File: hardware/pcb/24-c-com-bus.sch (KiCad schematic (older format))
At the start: 5 parts

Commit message: Created variants
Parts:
- C401: renamed from C?; Config (none) -> -MASTER
- R401: renamed from R?; Config (none) -> -MASTER,-SLAVE
- gave numbers to parts that had none: 3
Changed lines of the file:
@@
 EESchema Schematic File Version 4
-EELAYER 30 0
+LIBS:24-clocks-cache
+EELAYER 29 0
 EELAYER END
 $Descr A4 11693 8268
 encoding utf-8
-Sheet 3 7
+Sheet 4 7
 Title "24 Clocks"
 Date "2020-12-06"
@@
 P 5650 2950
 AR Path="/5FD2E1EF" Ref="U?"  Part="1"
-AR Path="/5FD135B5/5FD2E1EF" Ref="U?"  Part="1"
-F 0 "U?" H 5400 3450 50  0000 C CNN
+AR Path="/5FD135B5/5FD2E1EF" Ref="U401"  Part="1"
+F 0 "U401" H 5400 3450 50  0000 C CNN
 F 1 "MAX3485" H 5900 2400 50  0000 C CNN
 F 2 "" H 5650 2250 50  0001 C CNN
@@
 P 7700 2050
 AR Path="/5FD2E1FE" Ref="J?"  Part="1"
-AR Path="/5FD135B5/5FD2E1FE" Ref="J?"  Part="1"
-F 0 "J?" H 7850 1900 50  0000 C CNN
+AR Path="/5FD135B5/5FD2E1FE" Ref="J402"  Part="1"
+F 0 "J402" H 7850 1900 50  0000 C CNN
 F 1 "Conn_01x04" H 8050 2000 50  0000 C CNN
 F 2 "" H 7700 2050 50  0001 C CNN
@@
 P 5650 2400
 AR Path="/5FD2E204" Ref="#PWR?"  Part="1"
-AR Path="/5FD135B5/5FD2E204" Ref="#PWR?"  Part="1"
-F 0 "#PWR?" H 5650 2250 50  0001 C CNN
+AR Path="/5FD135B5/5FD2E204" Ref="#PWR0405"  Part="1"
+F 0 "#PWR0405" H 5650 2250 50  0001 C CNN
 F 1 "+3V3" H 5665 2573 50  0000 C CNN
 F 2 "" H 5650 2400 50  0001 C CNN
@@
 P 5650 3600
 AR Path="/5FD2E20A" Ref="#PWR?"  Part="1"
-AR Path="/5FD135B5/5FD2E20A" Ref="#PWR?"  Part="1"
-F 0 "#PWR?" H 5650 3350 50  0001 C CNN
+AR Path="/5FD135B5/5FD2E20A" Ref="#PWR0407"  Part="1"
+F 0 "#PWR0407" H 5650 3350 50  0001 C CNN
 F 1 "GND" H 5655 3427 50  0000 C CNN
 F 2 "" H 5650 3600 50  0001 C CNN
@@
 P 7450 2200
 AR Path="/5FD2E211" Ref="#PWR?"  Part="1"
-AR Path="/5FD135B5/5FD2E211" Ref="#PWR?"  Part="1"
-F 0 "#PWR?" H 7450 1950 50  0001 C CNN
+AR Path="/5FD135B5/5FD2E211" Ref="#PWR0404"  Part="1"
+F 0 "#PWR0404" H 7450 1950 50  0001 C CNN
 F 1 "GND" H 7455 2027 50  0000 C CNN
 F 2 "" H 7450 2200 50  0001 C CNN
@@
 P 7450 1800
 AR Path="/5FD2E217" Ref="#PWR?"  Part="1"
-AR Path="/5FD135B5/5FD2E217" Ref="#PWR?"  Part="1"
-F 0 "#PWR?" H 7450 1650 50  0001 C CNN
+AR Path="/5FD135B5/5FD2E217" Ref="#PWR0402"  Part="1"
+F 0 "#PWR0402" H 7450 1650 50  0001 C CNN
 F 1 "+9V" H 7465 1973 50  0000 C CNN
 F 2 "" H 7450 1800 50  0001 C CNN
@@
 P 6150 3000
 AR Path="/5FD2E221" Ref="R?"  Part="1"
-AR Path="/5FD135B5/5FD2E221" Ref="R?"  Part="1"
-F 0 "R?" H 6220 3046 50  0000 L CNN
+AR Path="/5FD135B5/5FD2E221" Ref="R401"  Part="1"
+F 0 "R401" H 6220 3046 50  0000 L CNN
 F 1 "R" H 6220 2955 50  0000 L CNN
 F 2 "" V 6080 3000 50  0001 C CNN
 F 3 "~" H 6150 3000 50  0001 C CNN
+F 4 "-MASTER,-SLAVE" H 6150 3000 50  0001 C CNN "Config"
 	1    6150 3000
 	1    0    0    -1
@@
 P 5050 3650
 AR Path="/5FD2E227" Ref="C?"  Part="1"
-AR Path="/5FD135B5/5FD2E227" Ref="C?"  Part="1"
-F 0 "C?" H 5165 3696 50  0000 L CNN
+AR Path="/5FD135B5/5FD2E227" Ref="C401"  Part="1"
+F 0 "C401" H 5165 3696 50  0000 L CNN
 F 1 "100nF" H 5165 3605 50  0000 L CNN
 F 2 "C0603" H 5088 3500 50  0001 C CNN
 F 3 "~" H 5050 3650 50  0001 C CNN
+F 4 "-MASTER" H 5050 3650 50  0001 C CNN "Config"
 	1    5050 3650
 	1    0    0    -1
@@
 P 6100 2050
 AR Path="/5FD2E22D" Ref="J?"  Part="1"
-AR Path="/5FD135B5/5FD2E22D" Ref="J?"  Part="1"
-F 0 "J?" H 6200 1900 50  0000 L CNN
+AR Path="/5FD135B5/5FD2E22D" Ref="J401"  Part="1"
+F 0 "J401" H 6200 1900 50  0000 L CNN
 F 1 "Conn_01x04" H 6200 2000 50  0000 L CNN
 F 2 "" H 6100 2050 50  0001 C CNN
@@
 P 6350 2200
 AR Path="/5FD2E233" Ref="#PWR?"  Part="1"
-AR Path="/5FD135B5/5FD2E233" Ref="#PWR?"  Part="1"
-F 0 "#PWR?" H 6350 1950 50  0001 C CNN
+AR Path="/5FD135B5/5FD2E233" Ref="#PWR0403"  Part="1"
+F 0 "#PWR0403" H 6350 1950 50  0001 C CNN
 F 1 "GND" H 6355 2027 50  0000 C CNN
 F 2 "" H 6350 2200 50  0001 C CNN
@@
 P 6350 1800
 AR Path="/5FD2E239" Ref="#PWR?"  Part="1"
-AR Path="/5FD135B5/5FD2E239" Ref="#PWR?"  Part="1"
-F 0 "#PWR?" H 6350 1650 50  0001 C CNN
+AR Path="/5FD135B5/5FD2E239" Ref="#PWR0401"  Part="1"
+F 0 "#PWR0401" H 6350 1650 50  0001 C CNN
 F 1 "+9V" H 6365 1973 50  0000 C CNN
 F 2 "" H 6350 1800 50  0001 C CNN
@@
 P 5050 3450
 AR Path="/5FD2E253" Ref="#PWR?"  Part="1"
-AR Path="/5FD135B5/5FD2E253" Ref="#PWR?"  Part="1"
-F 0 "#PWR?" H 5050 3300 50  0001 C CNN
+AR Path="/5FD135B5/5FD2E253" Ref="#PWR0406"  Part="1"
+F 0 "#PWR0406" H 5050 3300 50  0001 C CNN
 F 1 "+3V3" H 5065 3623 50  0000 C CNN
 F 2 "" H 5050 3450 50  0001 C CNN
@@
 P 5050 3850
 AR Path="/5FD2E259" Ref="#PWR?"  Part="1"
-AR Path="/5FD135B5/5FD2E259" Ref="#PWR?"  Part="1"
-F 0 "#PWR?" H 5050 3600 50  0001 C CNN
+AR Path="/5FD135B5/5FD2E259" Ref="#PWR0408"  Part="1"
+F 0 "#PWR0408" H 5050 3600 50  0001 C CNN
 F 1 "GND" H 5055 3677 50  0000 C CNN
 F 2 "" H 5050 3850 50  0001 C CNN

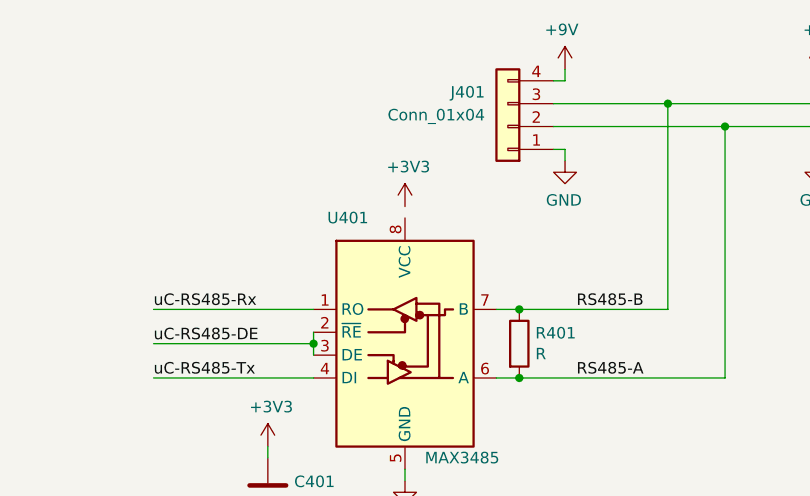
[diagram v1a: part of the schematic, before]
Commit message: Changed uC
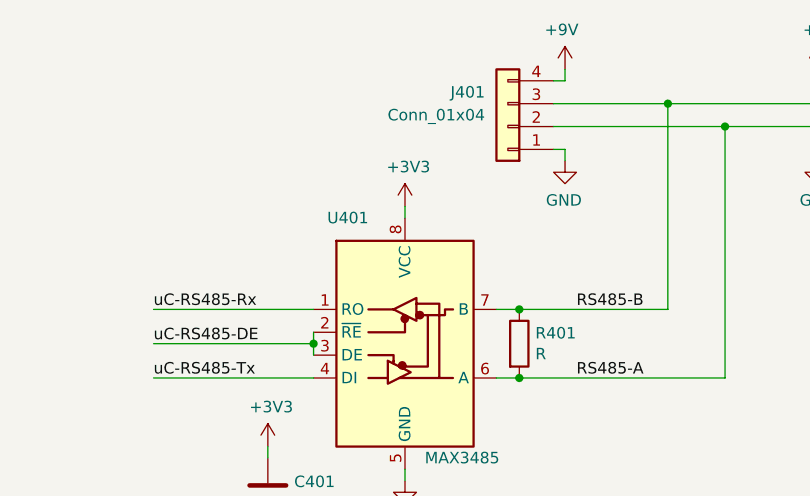
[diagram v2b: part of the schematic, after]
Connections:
- net +3V3: now also U401.8 (VCC)
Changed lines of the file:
@@
 EESchema Schematic File Version 4
-LIBS:24-clocks-cache
-EELAYER 29 0
+EELAYER 30 0
 EELAYER END
 $Descr A4 11693 8268
@@
 Text Label 3000 2550 2    50   ~ 0
 uC-RS485-DE
+Wire Wire Line
+	5650 2450 5650 2400
 $EndSCHEMATC

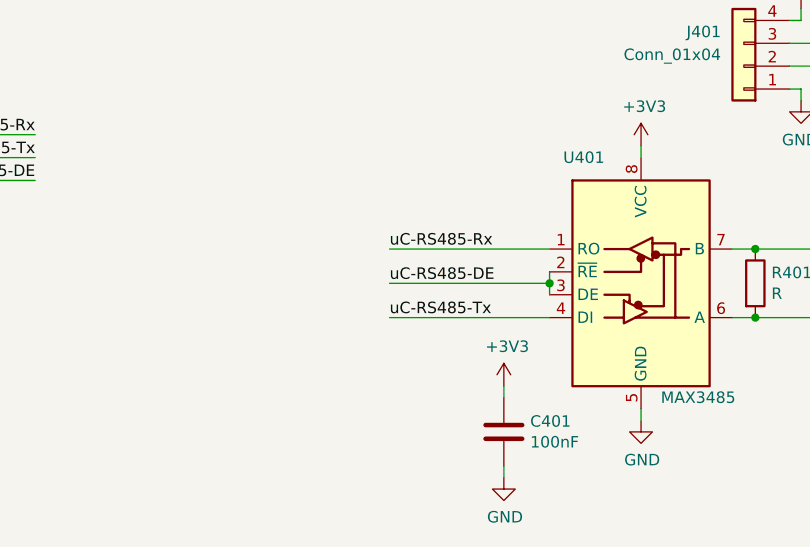
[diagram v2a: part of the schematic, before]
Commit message: Updated processor pins and added testpoints
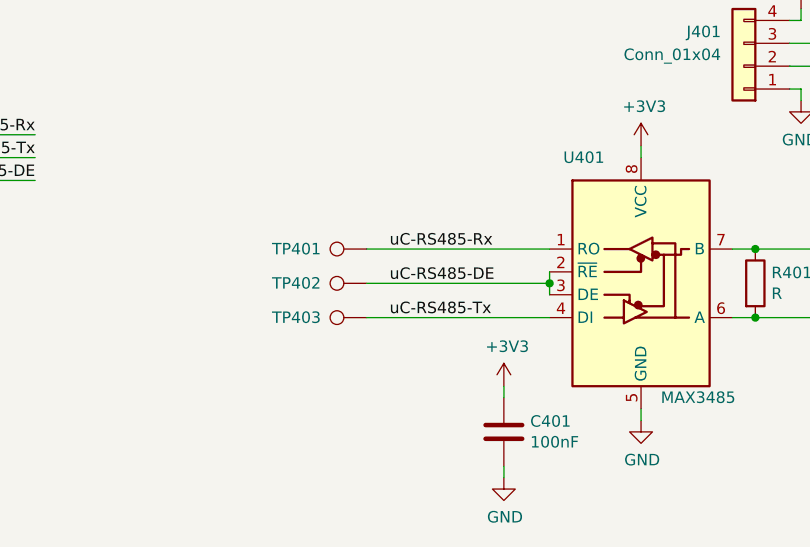
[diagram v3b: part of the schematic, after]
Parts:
- added TP401: uC-RS485-Rx, symbol Connector:TestPoint
- added TP402: uC-RS485-DE, symbol Connector:TestPoint
- added TP403: uC-RS485-Tx, symbol Connector:TestPoint
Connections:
- net uC-RS485-DE: now also TP402.1
- net uC-RS485-Rx: now also TP401.1
- net uC-RS485-Tx: now also TP403.1
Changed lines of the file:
@@
 $EndComp
-Wire Wire Line
-	4550 2850 5250 2850
-Wire Wire Line
-	4550 3000 5250 3000
-Wire Wire Line
-	4550 3150 5250 3150
 Wire Wire Line
 	5250 3050 5250 3000
@@
 Wire Wire Line
 	5650 2450 5650 2400
+$Comp
+L Connector:TestPoint TP401
+U 1 1 5FFCAC49
+P 4450 2850
+F 0 "TP401" V 4450 3050 50  0000 L CNN
+F 1 "uC-RS485-Rx" V 4554 2922 50  0001 C CNN
+F 2 "" H 4650 2850 50  0001 C CNN
+F 3 "~" H 4650 2850 50  0001 C CNN
+	1    4450 2850
+	0    -1   -1   0
+$EndComp
+$Comp
+L Connector:TestPoint TP402
+U 1 1 5FFCBD49
+P 4450 3000
+F 0 "TP402" V 4450 3200 50  0000 L CNN
+F 1 "uC-RS485-DE" V 4554 3072 50  0001 C CNN
+F 2 "" H 4650 3000 50  0001 C CNN
+F 3 "~" H 4650 3000 50  0001 C CNN
+	1    4450 3000
+	0    -1   -1   0
+$EndComp
+$Comp
+L Connector:TestPoint TP403
+U 1 1 5FFCBF72
+P 4450 3150
+F 0 "TP403" V 4450 3350 50  0000 L CNN
+F 1 "uC-RS485-Tx" V 4554 3222 50  0001 C CNN
+F 2 "" H 4650 3150 50  0001 C CNN
+F 3 "~" H 4650 3150 50  0001 C CNN
+	1    4450 3150
+	0    -1   -1   0
+$EndComp
+Wire Wire Line
+	4450 2850 5250 2850
+Wire Wire Line
+	4450 3000 5250 3000
+Wire Wire Line
+	4450 3150 5250 3150
 $EndSCHEMATC

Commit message: Small changes
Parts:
- R401: value R -> 120E
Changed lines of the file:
@@
 EESchema Schematic File Version 4
-EELAYER 30 0
+LIBS:24-clocks-cache
+EELAYER 29 0
 EELAYER END
 $Descr A4 11693 8268
@@
 AR Path="/5FD135B5/5FD2E221" Ref="R401"  Part="1"
 F 0 "R401" H 6220 3046 50  0000 L CNN
-F 1 "R" H 6220 2955 50  0000 L CNN
+F 1 "120E" H 6220 2955 50  0000 L CNN
 F 2 "" V 6080 3000 50  0001 C CNN
 F 3 "~" H 6150 3000 50  0001 C CNN

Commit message: Updated footprints
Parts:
- C401: footprint C0603 -> Capacitor_SMD:C_0603_1608Metric
- J401, J402: footprint (none) -> Connector_PinHeader_2.54mm:PinHeader_1x04_P2.54mm_Vertical
- R401: footprint (none) -> Resistor_SMD:R_0603_1608Metric
- TP401, TP402, TP403: footprint (none) -> TestPoint:TestPoint_Pad_1.5x1.5mm
- U401: footprint (none) -> Package_SO:SO-8_3.9x4.9mm_P1.27mm
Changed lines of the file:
@@
 F 0 "U401" H 5400 3450 50  0000 C CNN
 F 1 "MAX3485" H 5900 2400 50  0000 C CNN
-F 2 "" H 5650 2250 50  0001 C CNN
+F 2 "Package_SO:SO-8_3.9x4.9mm_P1.27mm" H 5650 2250 50  0001 C CNN
 F 3 "https://datasheets.maximintegrated.com/en/ds/MAX3483-MAX3491.pdf" H 5650 3000 50  0001 C CNN
 	1    5650 2950
@@
 F 0 "J402" H 7850 1900 50  0000 C CNN
 F 1 "Conn_01x04" H 8050 2000 50  0000 C CNN
-F 2 "" H 7700 2050 50  0001 C CNN
+F 2 "Connector_PinHeader_2.54mm:PinHeader_1x04_P2.54mm_Vertical" H 7700 2050 50  0001 C CNN
 F 3 "~" H 7700 2050 50  0001 C CNN
 	1    7700 2050
@@
 F 0 "R401" H 6220 3046 50  0000 L CNN
 F 1 "120E" H 6220 2955 50  0000 L CNN
-F 2 "" V 6080 3000 50  0001 C CNN
+F 2 "Resistor_SMD:R_0603_1608Metric" V 6080 3000 50  0001 C CNN
 F 3 "~" H 6150 3000 50  0001 C CNN
 F 4 "-MASTER,-SLAVE" H 6150 3000 50  0001 C CNN "Config"
@@
 F 0 "C401" H 5165 3696 50  0000 L CNN
 F 1 "100nF" H 5165 3605 50  0000 L CNN
-F 2 "C0603" H 5088 3500 50  0001 C CNN
+F 2 "Capacitor_SMD:C_0603_1608Metric" H 5088 3500 50  0001 C CNN
 F 3 "~" H 5050 3650 50  0001 C CNN
 F 4 "-MASTER" H 5050 3650 50  0001 C CNN "Config"
@@
 F 0 "J401" H 6200 1900 50  0000 L CNN
 F 1 "Conn_01x04" H 6200 2000 50  0000 L CNN
-F 2 "" H 6100 2050 50  0001 C CNN
+F 2 "Connector_PinHeader_2.54mm:PinHeader_1x04_P2.54mm_Vertical" H 6100 2050 50  0001 C CNN
 F 3 "~" H 6100 2050 50  0001 C CNN
 	1    6100 2050
@@
 F 0 "TP401" V 4450 3050 50  0000 L CNN
 F 1 "uC-RS485-Rx" V 4554 2922 50  0001 C CNN
-F 2 "" H 4650 2850 50  0001 C CNN
+F 2 "TestPoint:TestPoint_Pad_1.5x1.5mm" H 4650 2850 50  0001 C CNN
 F 3 "~" H 4650 2850 50  0001 C CNN
 	1    4450 2850
@@
 F 0 "TP402" V 4450 3200 50  0000 L CNN
 F 1 "uC-RS485-DE" V 4554 3072 50  0001 C CNN
-F 2 "" H 4650 3000 50  0001 C CNN
+F 2 "TestPoint:TestPoint_Pad_1.5x1.5mm" H 4650 3000 50  0001 C CNN
 F 3 "~" H 4650 3000 50  0001 C CNN
 	1    4450 3000
@@
 F 0 "TP403" V 4450 3350 50  0000 L CNN
 F 1 "uC-RS485-Tx" V 4554 3222 50  0001 C CNN
-F 2 "" H 4650 3150 50  0001 C CNN
+F 2 "TestPoint:TestPoint_Pad_1.5x1.5mm" H 4650 3150 50  0001 C CNN
 F 3 "~" H 4650 3150 50  0001 C CNN
 	1    4450 3150

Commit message: Added motor footprint, made init pcb
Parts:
- J401, J402: footprint Connector_PinHeader_2.54mm:PinHeader_1x04_P2.54mm_Vertical -> Connector_PinHeader_2.54mm:PinHeader_1x04_P2.54mm_Horizontal
- TP401, TP402, TP403: footprint TestPoint:TestPoint_Pad_1.5x1.5mm -> TestPoint:TestPoint_Pad_D2.0mm
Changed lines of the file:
@@
 F 0 "J402" H 7850 1900 50  0000 C CNN
 F 1 "Conn_01x04" H 8050 2000 50  0000 C CNN
-F 2 "Connector_PinHeader_2.54mm:PinHeader_1x04_P2.54mm_Vertical" H 7700 2050 50  0001 C CNN
+F 2 "Connector_PinHeader_2.54mm:PinHeader_1x04_P2.54mm_Horizontal" H 7700 2050 50  0001 C CNN
 F 3 "~" H 7700 2050 50  0001 C CNN
 	1    7700 2050
@@
 F 0 "J401" H 6200 1900 50  0000 L CNN
 F 1 "Conn_01x04" H 6200 2000 50  0000 L CNN
-F 2 "Connector_PinHeader_2.54mm:PinHeader_1x04_P2.54mm_Vertical" H 6100 2050 50  0001 C CNN
+F 2 "Connector_PinHeader_2.54mm:PinHeader_1x04_P2.54mm_Horizontal" H 6100 2050 50  0001 C CNN
 F 3 "~" H 6100 2050 50  0001 C CNN
 	1    6100 2050
@@
 F 0 "TP401" V 4450 3050 50  0000 L CNN
 F 1 "uC-RS485-Rx" V 4554 2922 50  0001 C CNN
-F 2 "TestPoint:TestPoint_Pad_1.5x1.5mm" H 4650 2850 50  0001 C CNN
+F 2 "TestPoint:TestPoint_Pad_D2.0mm" H 4650 2850 50  0001 C CNN
 F 3 "~" H 4650 2850 50  0001 C CNN
 	1    4450 2850
@@
 F 0 "TP402" V 4450 3200 50  0000 L CNN
 F 1 "uC-RS485-DE" V 4554 3072 50  0001 C CNN
-F 2 "TestPoint:TestPoint_Pad_1.5x1.5mm" H 4650 3000 50  0001 C CNN
+F 2 "TestPoint:TestPoint_Pad_D2.0mm" H 4650 3000 50  0001 C CNN
 F 3 "~" H 4650 3000 50  0001 C CNN
 	1    4450 3000
@@
 F 0 "TP403" V 4450 3350 50  0000 L CNN
 F 1 "uC-RS485-Tx" V 4554 3222 50  0001 C CNN
-F 2 "TestPoint:TestPoint_Pad_1.5x1.5mm" H 4650 3150 50  0001 C CNN
+F 2 "TestPoint:TestPoint_Pad_D2.0mm" H 4650 3150 50  0001 C CNN
 F 3 "~" H 4650 3150 50  0001 C CNN
 	1    4450 3150

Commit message: Finished PCB (#3)
* Created PCB outline and first placement

* Changed connectors

* Minor

* Included all 3D files

* Mixed changes

* Changed supply to 7V

* Archived PCB project

* Update 24-clocks-rescue.lib

* First placement

* Routed supplies

* Update 24-clocks.kicad_pcb

* Added routing

* Routed more nets

* Finished routing

* Archived project

* Replace hash and date

* minor

* Update pcb.yml

* Update pcb.yml

* Update pcb.yml

* Update pcb.yml

* Auto update commit date and hash

* Update output

* changed outputs

* Added layer to output

* Update hash and date also in sch

* Added caps to hall sensors

* Cleanup files
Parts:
- added D401: PESD1CAN, Package_TO_SOT_SMD:SOT-23, symbol 24-clocks-rescue:PESD1CAN-SparkFun-DiscreteSemi
- C401: Config -MASTER -> (none)
- J401, J402: value Conn_01x04 -> S4B_XH_SM4_TB; footprint Connector_PinHeader_2.54mm:PinHeader_1x04_P2.54mm_Horizontal -> mvl-footprints:JST_S4B_XH_SM4_TB
- R401: Config -MASTER,-SLAVE -> -SLAVE
- U401: footprint Package_SO:SO-8_3.9x4.9mm_P1.27mm -> Package_SO:SOIC-8_3.9x4.9mm_P1.27mm
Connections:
- net GND: now also D401.3
- net RS485-A: now also D401.1
- net RS485-B: now also D401.2
- net +9V renamed +7.5V
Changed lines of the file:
@@
 EESchema Schematic File Version 4
-LIBS:24-clocks-cache
-EELAYER 29 0
+EELAYER 30 0
 EELAYER END
 $Descr A4 11693 8268
@@
 Sheet 4 7
 Title "24 Clocks"
-Date "2020-12-06"
-Rev "V0.x"
+Date "GITDATE"
+Rev "GITHASH"
 Comp "Martin van Leussen"
 Comment1 ""
@@
 F 0 "U401" H 5400 3450 50  0000 C CNN
 F 1 "MAX3485" H 5900 2400 50  0000 C CNN
-F 2 "Package_SO:SO-8_3.9x4.9mm_P1.27mm" H 5650 2250 50  0001 C CNN
+F 2 "Package_SO:SOIC-8_3.9x4.9mm_P1.27mm" H 5650 2250 50  0001 C CNN
 F 3 "https://datasheets.maximintegrated.com/en/ds/MAX3483-MAX3491.pdf" H 5650 3000 50  0001 C CNN
 	1    5650 2950
@@
 AR Path="/5FD135B5/5FD2E1FE" Ref="J402"  Part="1"
 F 0 "J402" H 7850 1900 50  0000 C CNN
-F 1 "Conn_01x04" H 8050 2000 50  0000 C CNN
-F 2 "Connector_PinHeader_2.54mm:PinHeader_1x04_P2.54mm_Horizontal" H 7700 2050 50  0001 C CNN
-F 3 "~" H 7700 2050 50  0001 C CNN
+F 1 "S4B_XH_SM4_TB" H 8050 2000 50  0000 C CNN
+F 2 "mvl-footprints:JST_S4B_XH_SM4_TB" H 7700 2050 50  0001 C CNN
+F 3 "http://www.jst-mfg.com/product/pdf/eng/eXH.pdf" H 7700 2050 50  0001 C CNN
 	1    7700 2050
 	1    0    0    1
@@
 	1    0    0    -1
 $EndComp
-$Comp
-L power:+9V #PWR?
-U 1 1 5FD2E217
-P 7450 1800
-AR Path="/5FD2E217" Ref="#PWR?"  Part="1"
-AR Path="/5FD135B5/5FD2E217" Ref="#PWR0402"  Part="1"
-F 0 "#PWR0402" H 7450 1650 50  0001 C CNN
-F 1 "+9V" H 7465 1973 50  0000 C CNN
-F 2 "" H 7450 1800 50  0001 C CNN
-F 3 "" H 7450 1800 50  0001 C CNN
-	1    7450 1800
-	1    0    0    -1
-$EndComp
 Wire Wire Line
 	7450 1800 7450 1850
@@
 F 2 "Resistor_SMD:R_0603_1608Metric" V 6080 3000 50  0001 C CNN
 F 3 "~" H 6150 3000 50  0001 C CNN
-F 4 "-MASTER,-SLAVE" H 6150 3000 50  0001 C CNN "Config"
+F 4 "-SLAVE" H 6150 3000 50  0001 C CNN "Config"
 	1    6150 3000
 	1    0    0    -1
@@
 F 2 "Capacitor_SMD:C_0603_1608Metric" H 5088 3500 50  0001 C CNN
 F 3 "~" H 5050 3650 50  0001 C CNN
-F 4 "-MASTER" H 5050 3650 50  0001 C CNN "Config"
+F 4 "" H 5050 3650 50  0001 C CNN "Config"
 	1    5050 3650
 	1    0    0    -1
@@
 AR Path="/5FD135B5/5FD2E22D" Ref="J401"  Part="1"
 F 0 "J401" H 6200 1900 50  0000 L CNN
-F 1 "Conn_01x04" H 6200 2000 50  0000 L CNN
-F 2 "Connector_PinHeader_2.54mm:PinHeader_1x04_P2.54mm_Horizontal" H 6100 2050 50  0001 C CNN
-F 3 "~" H 6100 2050 50  0001 C CNN
+F 1 "S4B_XH_SM4_TB" H 6200 2000 50  0000 L CNN
+F 2 "mvl-footprints:JST_S4B_XH_SM4_TB" H 6100 2050 50  0001 C CNN
+F 3 "http://www.jst-mfg.com/product/pdf/eng/eXH.pdf" H 6100 2050 50  0001 C CNN
 	1    6100 2050
 	-1   0    0    1
@@
 	-1   0    0    -1
 $EndComp
-$Comp
-L power:+9V #PWR?
-U 1 1 5FD2E239
-P 6350 1800
-AR Path="/5FD2E239" Ref="#PWR?"  Part="1"
-AR Path="/5FD135B5/5FD2E239" Ref="#PWR0401"  Part="1"
-F 0 "#PWR0401" H 6350 1650 50  0001 C CNN
-F 1 "+9V" H 6365 1973 50  0000 C CNN
-F 2 "" H 6350 1800 50  0001 C CNN
-F 3 "" H 6350 1800 50  0001 C CNN
-	1    6350 1800
-	-1   0    0    -1
-$EndComp
 Wire Wire Line
 	6350 1800 6350 1850
@@
 	6300 1950 6800 1950
 Wire Wire Line
-	6300 2050 7050 2050
+	6300 2050 7000 2050
 Wire Wire Line
 	6800 2850 6800 1950
@@
 	6800 1950 7500 1950
 Wire Wire Line
-	7050 3150 7050 2050
-Connection ~ 7050 2050
-Wire Wire Line
-	7050 2050 7500 2050
+	7000 3150 7000 2050
+Connection ~ 7000 2050
+Wire Wire Line
+	7000 2050 7500 2050
 Text Label 6400 2850 0    50   ~ 0
 RS485-B
@@
 	6150 3150 6050 3150
 Wire Wire Line
-	6150 3150 7050 3150
+	6150 3150 7000 3150
 Wire Wire Line
 	6150 2850 6800 2850
@@
 Wire Wire Line
 	4450 3150 5250 3150
+$Comp
+L 24-clocks-rescue:PESD1CAN-SparkFun-DiscreteSemi D401
+U 1 1 5FEA3168
+P 6900 3550
+AR Path="/5FEA3168" Ref="D401"  Part="1"
+AR Path="/5FD135B5/5FEA3168" Ref="D401"  Part="1"
+F 0 "D401" V 6858 3778 45  0000 L CNN
+F 1 "PESD1CAN" V 6942 3778 45  0000 L CNN
+F 2 "Package_TO_SOT_SMD:SOT-23" H 6900 3900 20  0001 C CNN
+F 3 "https://assets.nexperia.com/documents/data-sheet/PESD1CAN.pdf" H 6900 3550 50  0001 C CNN
+	1    6900 3550
+	0    1    1    0
+$EndComp
+Wire Wire Line
+	6800 2850 6800 3250
+Connection ~ 6800 2850
+Wire Wire Line
+	7000 3150 7000 3250
+Connection ~ 7000 3150
+$Comp
+L power:GND #PWR?
+U 1 1 5FEA7BEF
+P 6900 3900
+AR Path="/5FEA7BEF" Ref="#PWR?"  Part="1"
+AR Path="/5FD135B5/5FEA7BEF" Ref="#PWR0409"  Part="1"
+F 0 "#PWR0409" H 6900 3650 50  0001 C CNN
+F 1 "GND" H 6905 3727 50  0000 C CNN
+F 2 "" H 6900 3900 50  0001 C CNN
+F 3 "" H 6900 3900 50  0001 C CNN
+	1    6900 3900
+	1    0    0    -1
+$EndComp
+Wire Wire Line
+	6900 3900 6900 3850
+$Comp
+L power:+7.5V #PWR0108
+U 1 1 6007755B
+P 6350 1800
+F 0 "#PWR0108" H 6350 1650 50  0001 C CNN
+F 1 "+7.5V" H 6365 1973 50  0000 C CNN
+F 2 "" H 6350 1800 50  0001 C CNN
+F 3 "" H 6350 1800 50  0001 C CNN
+	1    6350 1800
+	1    0    0    -1
+$EndComp
+$Comp
+L power:+7.5V #PWR0110
+U 1 1 60077F85
+P 7450 1800
+F 0 "#PWR0110" H 7450 1650 50  0001 C CNN
+F 1 "+7.5V" H 7465 1973 50  0000 C CNN
+F 2 "" H 7450 1800 50  0001 C CNN
+F 3 "" H 7450 1800 50  0001 C CNN
+	1    7450 1800
+	1    0    0    -1
+$EndComp
 $EndSCHEMATC
